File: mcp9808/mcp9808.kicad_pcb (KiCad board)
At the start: 4 copper layers, 21 parts, among them Q1 AO3400A, Q2 AO3400A, Q3 AO3400A, U1 MCP9808_MSOP

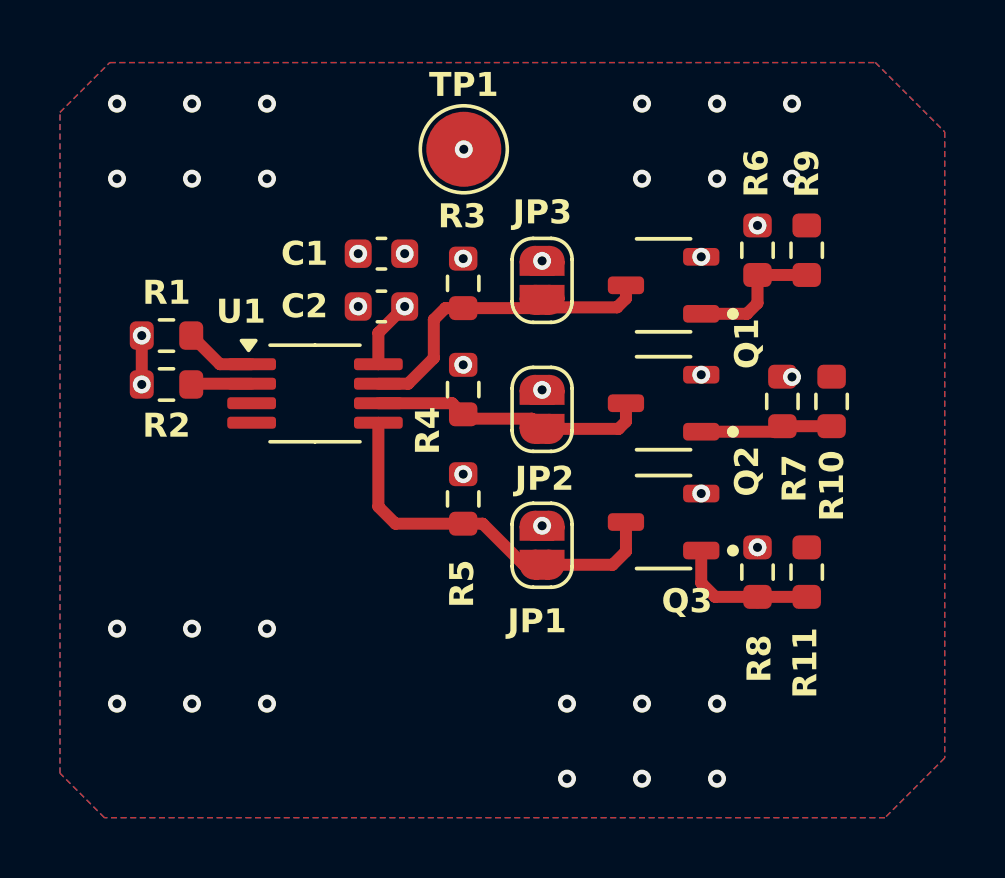
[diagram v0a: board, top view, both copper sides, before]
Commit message: [Rushil] added user drwaing for block outline, removed test point, reduced the size of block and solved white space issue
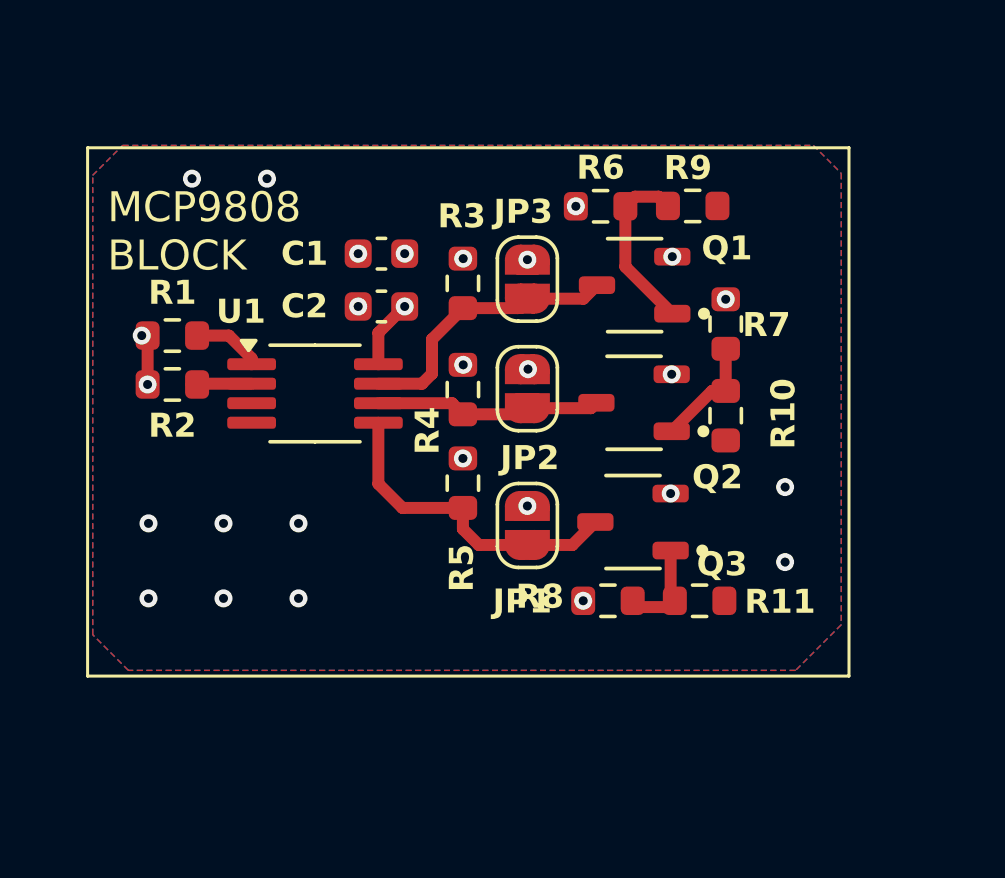
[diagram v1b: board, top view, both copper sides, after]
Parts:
- removed TP1: TestPoint, TestPoint:TestPoint_Pad_D2.5mm
- moved R6 5.43 mm to (136.1, 75.9), turned to 180 degrees
- moved R8 5.08 mm to (136.4, 89.1), turned to 180 degrees
- moved R9 4.08 mm to (139.2, 75.9), turned to 180 degrees
- moved R11 3.70 mm to (139.4, 89.1), turned to 180 degrees
- moved R10 3.56 mm to (140.3, 82.9), turned to 90 degrees
- moved R7 3.20 mm to (140.3, 79.8)
- moved Q3 1.02 mm to (137.2, 86.4)
- moved Q2 0.99 mm to (137.2, 82.5)
- moved Q1 0.97 mm to (137.3, 78.5)
- moved JP2 0.85 mm to (133.7, 82.0)
- moved JP1 0.82 mm to (133.7, 86.6)
- moved R5 0.53 mm to (131.5, 85.2)
- moved JP3 0.49 mm to (133.7, 78.3)
- moved R1 0.19 mm to (121.8, 80.2)
- moved R2 0.19 mm to (121.8, 81.9)
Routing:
- net /block_mcp9808/A2: track 13.0 -> 10.6 mm
- net Net-(Q3-Pad1): track 5.05 -> 3.31 mm
- net /block_mcp9808/A1: track 9.32 -> 7.59 mm
- net /block_mcp9808/A0: track 10.8 -> 9.33 mm
- net Net-(Q1-Pad1): track 4.60 -> 5.91 mm
- net Net-(Q2-Pad1): track 4.67 -> 3.76 mm
- net /block_mcp9808/VCC: vias 8 -> 7
- net /block_mcp9808/GND: vias 35 -> 21
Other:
- board text added: "MCP9808 BLOCK"

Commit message: [Rushil] removed mos, made more compact, designator resize according to constraints,default id on silk screen
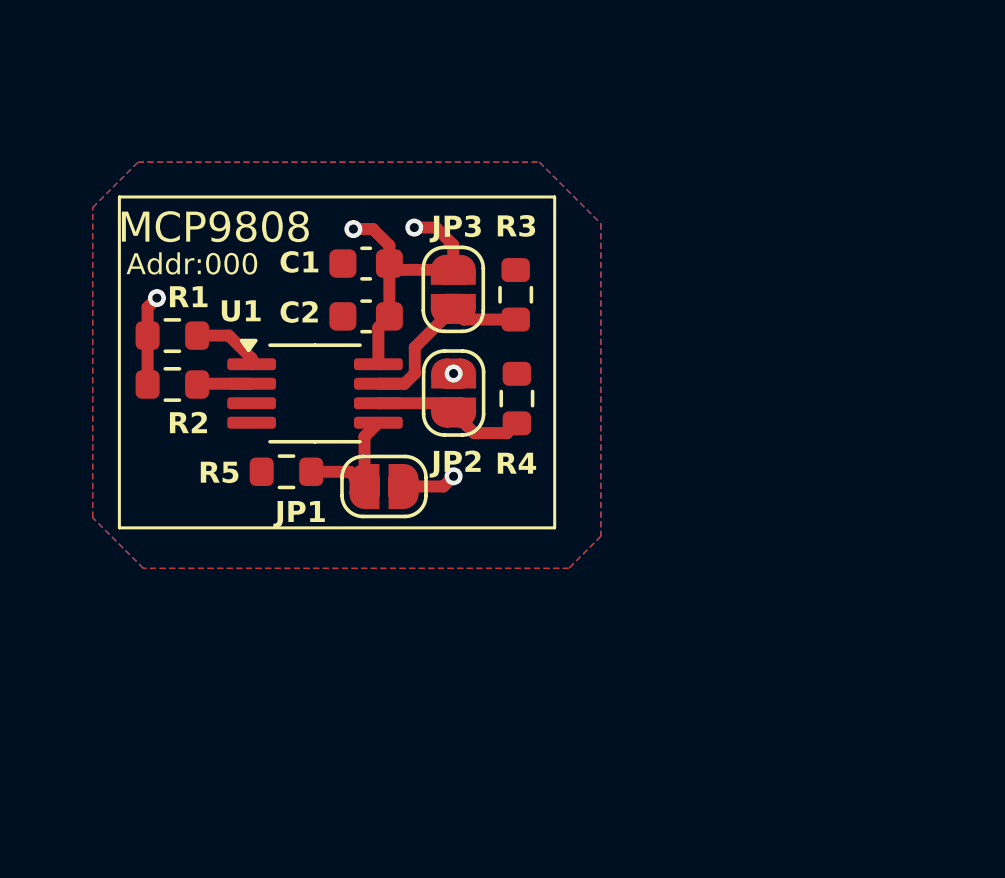
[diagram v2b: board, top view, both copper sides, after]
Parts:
- removed Q1, Q2, Q3: AO3400A, AO3400A:SOT95P280X125-3N
- removed R10, R11, R9: 100, Resistor_SMD:R_0603_1608Metric
- removed R6, R7, R8: 10k, Resistor_SMD:R_0603_1608Metric
- moved R5 5.89 mm to (125.7, 84.8), turned to 180 degrees
- moved JP1 4.95 mm to (128.9, 85.3), turned to 0 degrees
- moved JP3 2.49 mm to (131.2, 78.7), turned to 90 degrees
- moved JP2 2.46 mm to (131.2, 82.1), turned to 90 degrees
- moved R4 1.82 mm to (133.3, 82.3), turned to 90 degrees
- moved R3 1.80 mm to (133.3, 78.9), turned to 90 degrees
- moved C1 0.61 mm to (128.3, 77.8)
- moved C2 0.61 mm to (128.3, 79.6)
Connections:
- JP1 pad 1: /block_mcp9808/GND -> /block_mcp9808/A2
- JP1 pad 2: /block_mcp9808/A2 -> /block_mcp9808/VCC
- JP2 pad 1: /block_mcp9808/GND -> /block_mcp9808/A1
- JP2 pad 2: /block_mcp9808/A1 -> /block_mcp9808/VCC
- JP3 pad 1: /block_mcp9808/GND -> /block_mcp9808/A0
- JP3 pad 2: /block_mcp9808/A0 -> /block_mcp9808/VCC
- R3 pad 1: /block_mcp9808/VCC -> /block_mcp9808/A0
- R3 pad 2: /block_mcp9808/A0 -> /block_mcp9808/GND
- R4 pad 1: /block_mcp9808/VCC -> /block_mcp9808/A1
- R4 pad 2: /block_mcp9808/A1 -> /block_mcp9808/GND
- R5 pad 1: /block_mcp9808/VCC -> /block_mcp9808/A2
- R5 pad 2: /block_mcp9808/A2 -> /block_mcp9808/GND
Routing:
- net /block_mcp9808/VCC: track 3.92 -> 14.9 mm, vias 7 -> 5
- net /block_mcp9808/A2: track 10.6 -> 4.29 mm
- net Net-(Q1-Pad1): track 5.91 -> 0.00 mm
- net Net-(Q2-Pad1): track 3.76 -> 0.00 mm
- net Net-(Q3-Pad1): track 3.31 -> 0.00 mm
- net /block_mcp9808/A0: track 9.33 -> 6.27 mm
- net /block_mcp9808/A1: track 7.59 -> 5.16 mm
- net /block_mcp9808/GND: vias 21 -> 0
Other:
- board text added: "Addr:000"
- board text added: "MCP9808"
- board text removed: "MCP9808 BLOCK"

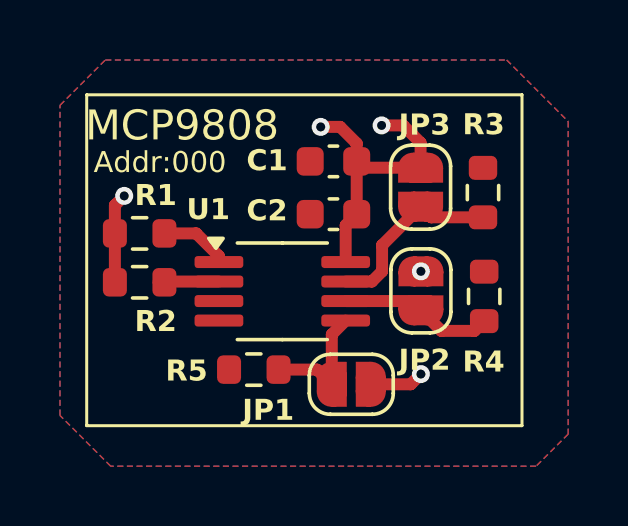
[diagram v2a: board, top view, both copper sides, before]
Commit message: [Rushil] address on silkscreen corrected and removed on pad vias
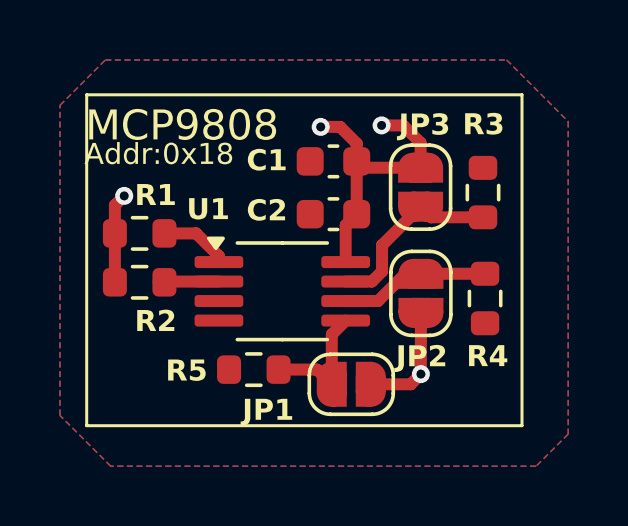
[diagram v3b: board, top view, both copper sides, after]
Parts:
- moved JP2 0.09 mm to (131.2, 82.2), turned to -90 degrees
- moved R4 0.08 mm to (133.4, 82.4), turned to -90 degrees
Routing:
- net /block_mcp9808/VCC: track 14.9 -> 17.0 mm, vias 5 -> 4
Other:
- board text added: "Addr:0x18"
- board text removed: "Addr:000"

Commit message: [Rushil] corrected pcb added information on both schematic and pcb user drawing correct circuit of bno055
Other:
- board text added: "It is a high-accuracy digital temperature sensor with I²C interface and configurable address pins, offering ±0.25°C precision"
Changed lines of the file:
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@@
+		)
+	)
+	(gr_text "It is a high-accuracy digital\ntemperature sensor with I²C \ninterface and configurable \naddress pins, offering ±0.25°C \nprecision"
+		(at 122.22 86.08 0)
+		(layer "Dwgs.User")
+		(effects
+			(font
+				(size 0.5 0.5)
+				(thickness 0.125)
+			)
+			(justify left bottom)
 		)
 	)
